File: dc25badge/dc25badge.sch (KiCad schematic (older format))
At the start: 35 parts, among them P1 BATT, P2 USB_OTG, P3 CONN_CORTEX, P4 UART, SW1 SW_Push, U1 MIC5305, U2 TPS61032, U3 ATSAMD21E18A-AU, U4 74AHCT125, Y1 32.768k

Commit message: First letter routed.
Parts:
- added C14: 100u, Capacitors_SMD:C_1206_HandSoldering, symbol CP1_Small
- added C27: 1u, Capacitors_SMD:C_0805_HandSoldering, symbol C_Small
- added SW2: PWR, Buttons_Switches_SMD:SW_SPST_EVQP0, symbol SW_Push
- added SW3: MODE, Buttons_Switches_SMD:SW_SPST_EVQP0, symbol SW_Push
- added SW4: BRIGHT, Buttons_Switches_SMD:SW_SPST_EVQP0, symbol SW_Push
- C1, C10, C11, C12, C13, C2, C3, C4, C7, C8, C9: footprint (none) -> Capacitors_SMD:C_0805_HandSoldering
- C5: value 2.2u -> 1u; footprint (none) -> Capacitors_SMD:C_0805_HandSoldering
- C6: value 220u -> 100u; footprint (none) -> Capacitors_SMD:C_1206_HandSoldering
- FB1, R1, R2, R3, R4, R5, R6, R7: footprint (none) -> Resistors_SMD:R_0805_HandSoldering
- L1: footprint (none) -> Choke_SMD:Choke_SMD_12x12mm_h4.5mm
- P1: footprint (none) -> Connectors_JST:JST_PH_S2B-PH-SM4-TB_02x2.00mm_Angled
- P2: footprint (none) -> Connectors:USB_Micro-B
- P3: footprint (none) -> Pin_Headers:Pin_Header_Straight_2x05_Pitch1.27mm_SMD
- P4: footprint (none) -> Pin_Headers:Pin_Header_Straight_1x03_Pitch2.54mm_SMD_Pin1Left
- SW1: value SW_Push -> RESET; footprint (none) -> Buttons_Switches_SMD:SW_SPST_EVQP0
- U1: footprint (none) -> TO_SOT_Packages_SMD:SOT-23-5
- U2: footprint (none) -> Badge_Parts:PowerPAD16
- U3: footprint (none) -> Housings_QFP:TQFP-32_7x7mm_Pitch0.8mm
- U4: footprint (none) -> SMD_Packages:SOIC-14_N
- W1, W2, W3: footprint (none) -> Measurement_Points:Measurement_Point_Round-SMD-Pad_Big
- Y1: footprint (none) -> Crystals:Crystal_SMD_G8
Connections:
- net labels added: BRIGHT, MODE, MOSI3, SCLK3, SOFT_PWR, SPI_EN
- wire segments 114 -> 126
- no-connect marks 24 -> 21
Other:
- moved on the sheet: C5, P1, R7, U4A, U4B

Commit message: remove old PS.
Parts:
- removed C14, C6: 100u, Capacitors_SMD:C_1206_HandSoldering, symbol CP1_Small
- removed C27, C5: 1u, Capacitors_SMD:C_0805_HandSoldering, symbol C_Small
- removed C4: 10u, Capacitors_SMD:C_0805_HandSoldering, symbol C_Small
- removed L1: 6.8uH, Choke_SMD:Choke_SMD_12x12mm_h4.5mm, symbol L_Core_Ferrite
- removed R1: 1.8M, Resistors_SMD:R_0805_HandSoldering, symbol R_Small
- removed R2: 330k, Resistors_SMD:R_0805_HandSoldering, symbol R_Small
- removed R3, R4: 10k, Resistors_SMD:R_0805_HandSoldering, symbol R_Small
- removed U2: TPS61032, Badge_Parts:PowerPAD16, symbol TPS61030
- P3: footprint Pin_Headers:Pin_Header_Straight_2x05_Pitch1.27mm_SMD -> Pin_Headers2:Pin_Header_Straight_2x05_Pitch1.27mm_SMD
- P4: footprint Pin_Headers:Pin_Header_Straight_1x03_Pitch2.54mm_SMD_Pin1Left -> Pin_Headers2:Pin_Header_Straight_1x03_Pitch2.54mm_SMD_Pin1Left
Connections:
- net labels removed: BAT_LO
- wire segments 126 -> 91
- no-connect marks 21 -> 20
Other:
- moved on the sheet: W1, W3

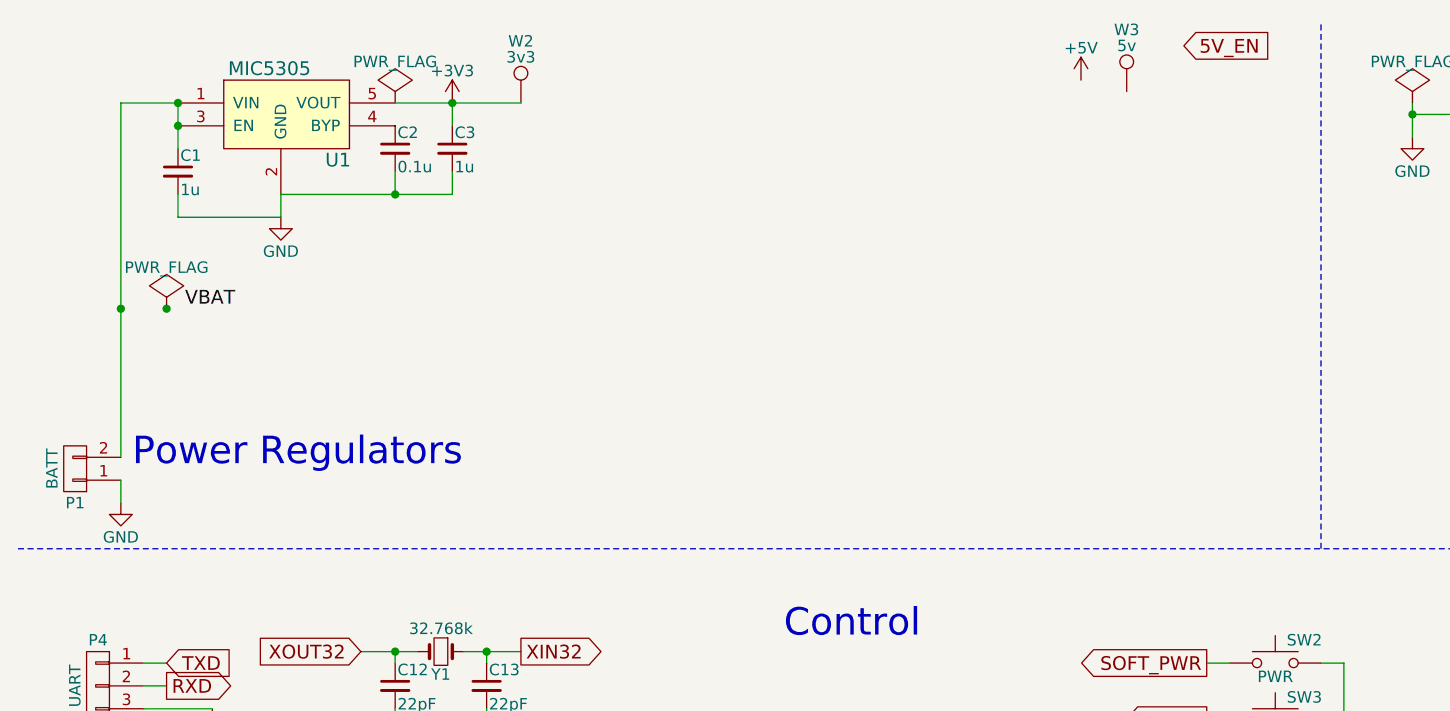
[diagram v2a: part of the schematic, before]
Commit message: schematic for new PS.
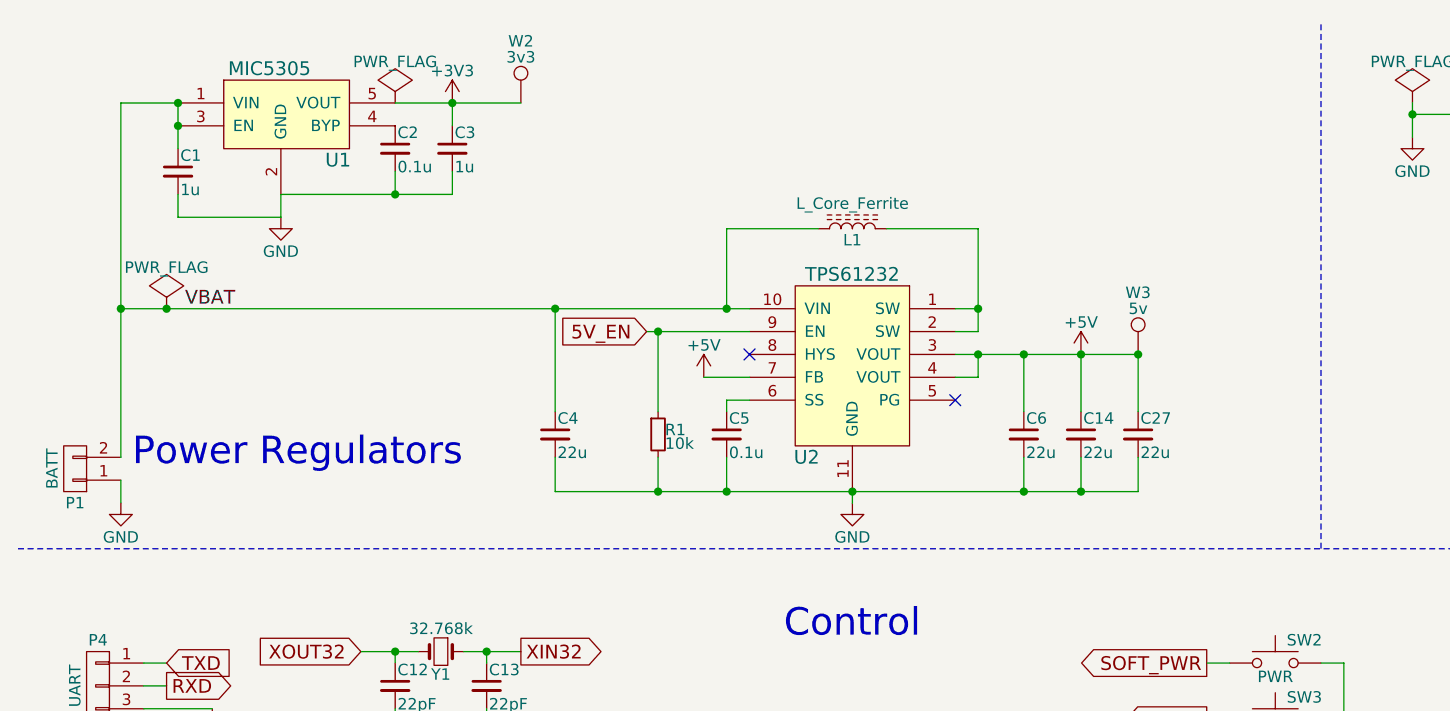
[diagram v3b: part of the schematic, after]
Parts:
- added C14, C27, C4, C6: 22u, symbol C_Small
- added C5: 0.1u, symbol C_Small
- added L1: L_Core_Ferrite, symbol L_Core_Ferrite
- added R1: 10k, symbol R_Small
- added U2: TPS61232, symbol TPS61232
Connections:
- wire segments 91 -> 118
- no-connect marks 20 -> 22
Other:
- moved on the sheet: W3

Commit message: Before routing back.
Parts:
- removed FB1: FB300, Resistors_SMD:R_0805_HandSoldering, symbol L_Small
- C14, C27, C4, C5, C6: footprint (none) -> Capacitors_SMD:C_0805_HandSoldering
- L1: footprint (none) -> Badge_Parts:Inductor_6.5x6
- P2: footprint Connectors:USB_Micro-B -> Badge_Parts:Amphenol_10118192
- R1: footprint (none) -> Resistors_SMD:R_0805_HandSoldering
- U2: footprint (none) -> Badge_Parts:PSON-10P
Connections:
- wire segments 118 -> 117
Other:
- moved on the sheet: W1

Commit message: Full routing.
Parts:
- removed P4: UART, Pin_Headers2:Pin_Header_Straight_1x03_Pitch2.54mm_SMD_Pin1Left, symbol CONN_01X03
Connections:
- net 5V_EN: now also U3.25 (PA27); no longer U3.5 (PA04)
- net GND: now also P2.6 (shield)
- net USBDM renamed USBD-
- net USBDP renamed USBD+
- no-connect marks 22 -> 24
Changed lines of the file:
@@
 SWCLK
 Text GLabel 3750 4450 2    60   BiDi ~ 0
-USBDM
+USBD-
 Text GLabel 3750 4350 2    60   BiDi ~ 0
-USBDP
+USBD+
 $Comp
 L USB_OTG P2
@@
 	1    0    0    -1
 $EndComp
-NoConn ~ 850  4350
 NoConn ~ 1250 4050
 NoConn ~ 1250 3750
 Text GLabel 1250 3850 2    60   BiDi ~ 0
-USBDM
+USBD-
 Text GLabel 1250 3950 2    60   BiDi ~ 0
-USBDP
+USBD+
 $Comp
 L 74AHCT125 U4
@@
 	2300 4850 2200 4850
 NoConn ~ 3650 4550
-Text GLabel 2200 4350 0    60   Output ~ 0
+Text GLabel 3750 4250 2    60   Output ~ 0
 5V_EN
-Wire Wire Line
-	2200 4350 2300 4350
-$Comp
-L CONN_01X03 P4
-U 1 1 592AFF5F
-P 850 3400
-F 0 "P4" H 850 3600 50  0000 C CNN
-F 1 "UART" V 950 3400 50  0000 C CNN
-F 2 "Pin_Headers2:Pin_Header_Straight_1x03_Pitch2.54mm_SMD_Pin1Left" H 850 3400 50  0001 C CNN
-F 3 "" H 850 3400 50  0000 C CNN
-	1    850  3400
-	-1   0    0    -1
-$EndComp
 $Comp
 L GND #PWR023
@@
 Connection ~ 5400 1950
 NoConn ~ 3650 4150
-NoConn ~ 3650 4250
 NoConn ~ 3650 4650
 Wire Wire Line
@@
 Wire Wire Line
 	2300 4650 2200 4650
+NoConn ~ 1050 3500
+NoConn ~ 1050 3400
+NoConn ~ 1050 3300
+$Comp
+L GND #PWR028
+U 1 1 592CB85E
+P 850 4400
+F 0 "#PWR028" H 850 4150 50  0001 C CNN
+F 1 "GND" H 850 4250 50  0000 C CNN
+F 2 "" H 850 4400 50  0000 C CNN
+F 3 "" H 850 4400 50  0000 C CNN
+	1    850  4400
+	1    0    0    -1
+$EndComp
+Wire Wire Line
+	850  4400 850  4350
+NoConn ~ 2300 4350
+Wire Wire Line
+	3750 4250 3650 4250
 $EndSCHEMATC

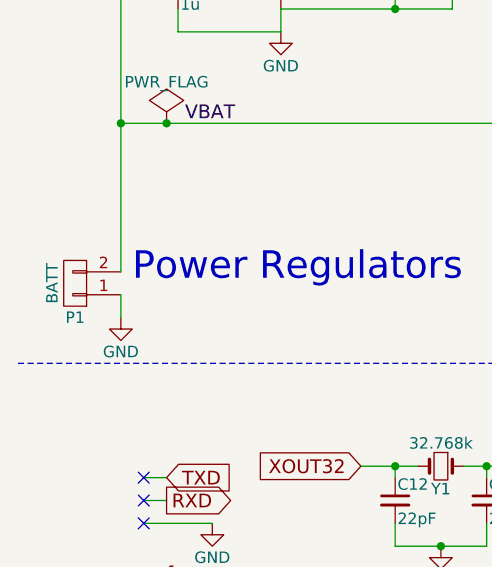
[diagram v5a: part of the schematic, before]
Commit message: Fix battery error.
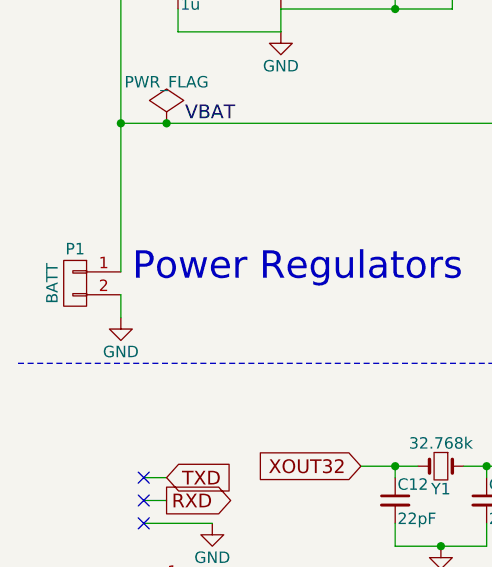
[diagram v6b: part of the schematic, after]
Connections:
- net GND: now also P1.2 (P2); no longer P1.1 (P1)
- net VBAT: now also P1.1 (P1); no longer P1.2 (P2)
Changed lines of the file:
@@
 F 3 "" H 750 2450 50  0000 C CNN
 	1    750  2450
-	-1   0    0    1
+	-1   0    0    -1
 $EndComp
 $Comp

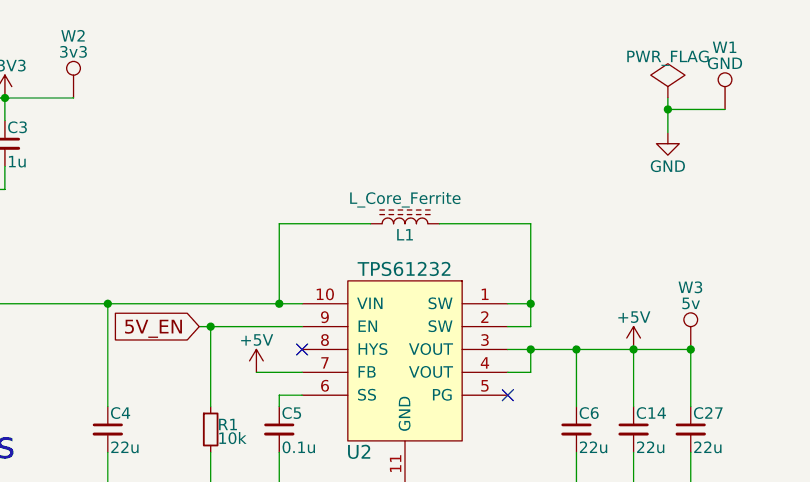
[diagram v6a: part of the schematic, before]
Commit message: Switch to 0603 caps on oscillator.
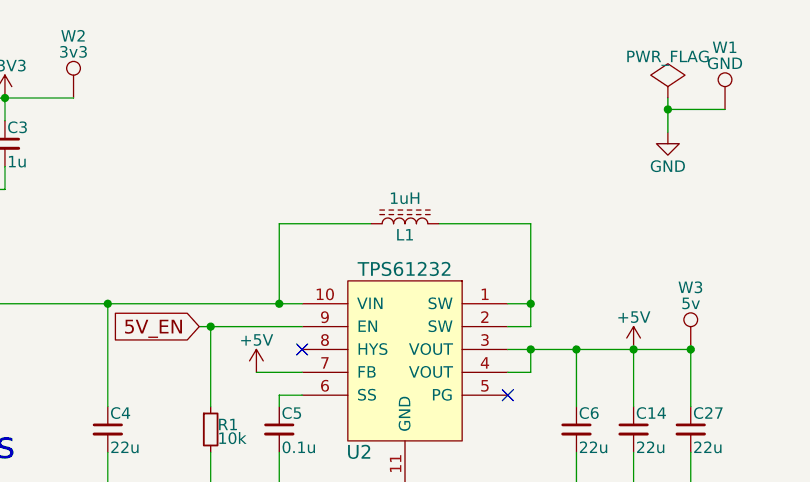
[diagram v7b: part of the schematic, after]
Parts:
- L1: value L_Core_Ferrite -> 1uH
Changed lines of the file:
@@
 P 4150 1400
 F 0 "L1" V 4100 1400 50  0000 C CNN
-F 1 "L_Core_Ferrite" V 4260 1400 50  0000 C CNN
+F 1 "1uH" V 4260 1400 50  0000 C CNN
 F 2 "Badge_Parts:Inductor_6.5x6" H 4150 1400 50  0001 C CNN
 F 3 "" H 4150 1400 50  0000 C CNN
